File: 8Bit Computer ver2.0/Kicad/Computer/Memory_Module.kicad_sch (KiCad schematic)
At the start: 23 parts, among them IC2 MP2338GTL-Z, J25 M20-8890845, J26 M20-8890845, J27 M20-8890845, J28 M20-8890845, J29 M20-8890845, J30 M20-8890845, J31 M20-8890845

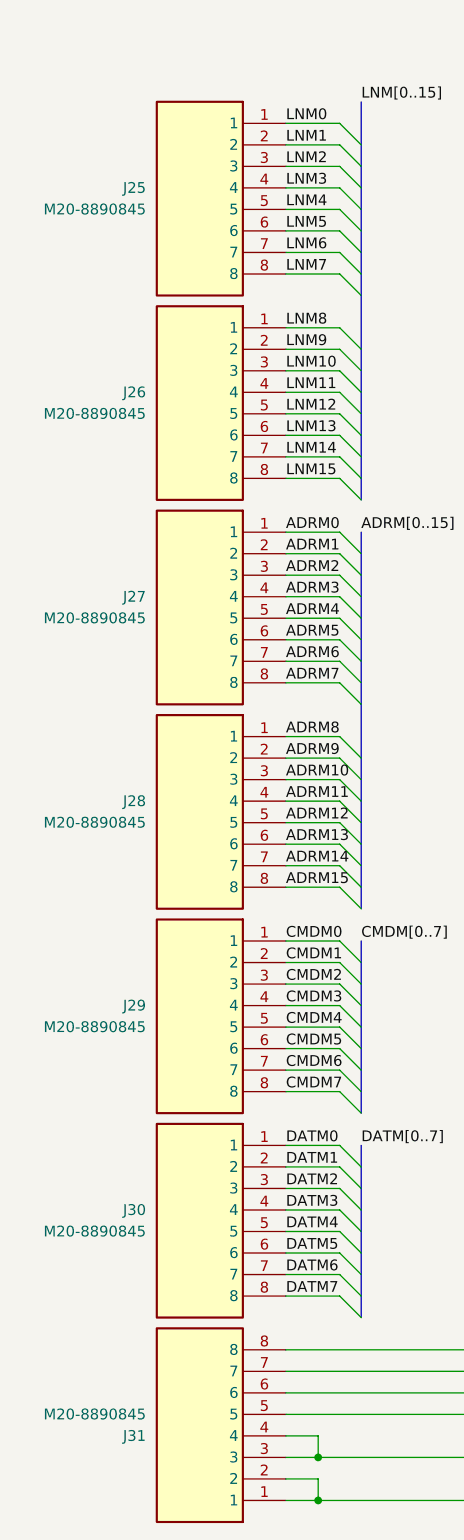
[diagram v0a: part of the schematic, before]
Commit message: changed page numbers, every schematic is now A4
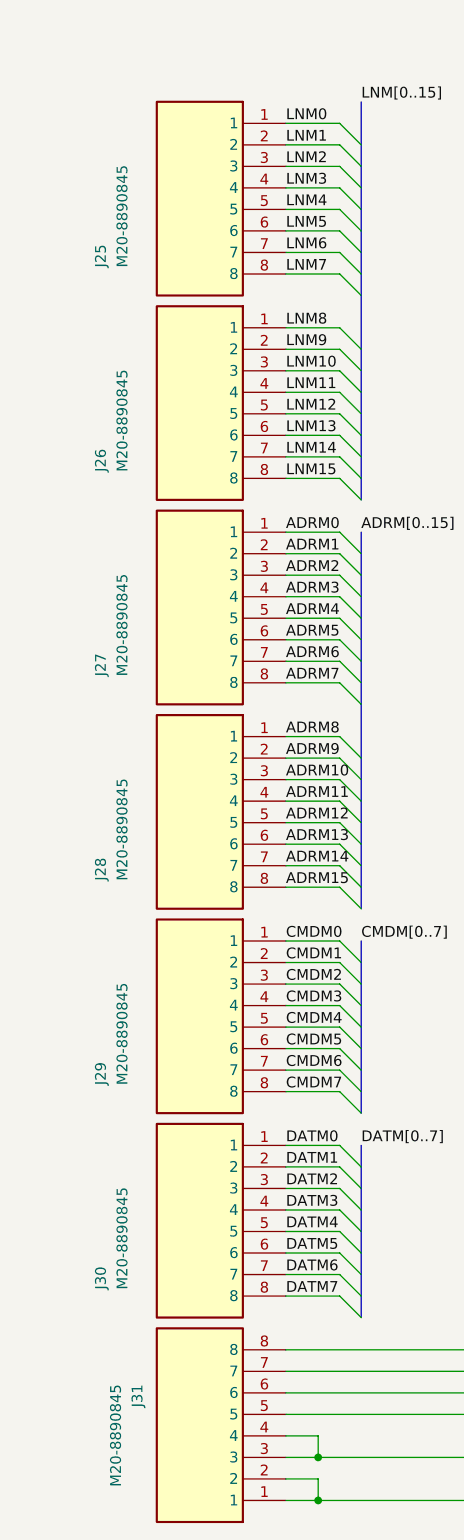
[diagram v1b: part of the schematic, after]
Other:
- title: (none) -> ${SHEETNAME}
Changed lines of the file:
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@@
 	(generator_version "9.0")
 	(paper "A4")
+	(title_block
+		(title "${SHEETNAME}")
+		(date "2026-03-21")
+		(rev "2.7")
+	)
 	(junction
 		(at 275.59 138.43)
@@
 		(dnp no)
 		(property "Reference" "J29"
-			(at 24.13 129.5399 0)
+			(at 18.796 138.938 90)
 			(effects
 				(font
@@
 		)
 		(property "Value" "M20-8890845"
-			(at 24.13 132.0799 0)
+			(at 21.336 138.938 90)
 			(effects
 				(font
@@
 		(dnp no)
 		(property "Reference" "J26"
-			(at 24.13 57.1499 0)
+			(at 18.796 66.548 90)
 			(effects
 				(font
@@
 		)
 		(property "Value" "M20-8890845"
-			(at 24.13 59.6899 0)
+			(at 21.336 66.548 90)
 			(effects
 				(font
@@
 		(dnp no)
 		(property "Reference" "J30"
-			(at 24.13 153.6699 0)
+			(at 18.796 163.068 90)
 			(effects
 				(font
@@
 		)
 		(property "Value" "M20-8890845"
-			(at 24.13 156.2099 0)
+			(at 21.336 163.068 90)
 			(effects
 				(font
@@
 		(dnp no)
 		(property "Reference" "J28"
-			(at 24.13 105.4099 0)
+			(at 18.796 114.808 90)
 			(effects
 				(font
@@
 		)
 		(property "Value" "M20-8890845"
-			(at 24.13 107.9499 0)
+			(at 21.336 114.808 90)
 			(effects
 				(font
@@
 		(dnp no)
 		(property "Reference" "J31"
-			(at 24.13 180.3401 0)
+			(at 23.114 174.244 90)
 			(effects
 				(font
@@
 		)
 		(property "Value" "M20-8890845"
-			(at 24.13 177.8001 0)
+			(at 20.574 174.244 90)
 			(effects
 				(font
@@
 		(dnp no)
 		(property "Reference" "J25"
-			(at 24.13 33.0199 0)
+			(at 18.796 42.418 90)
 			(effects
 				(font
@@
 		)
 		(property "Value" "M20-8890845"
-			(at 24.13 35.5599 0)
+			(at 21.336 42.418 90)
 			(effects
 				(font
@@
 		(dnp no)
 		(property "Reference" "J27"
-			(at 24.13 81.2799 0)
+			(at 18.796 90.678 90)
 			(effects
 				(font
@@
 		)
 		(property "Value" "M20-8890845"
-			(at 24.13 83.8199 0)
+			(at 21.336 90.678 90)
 			(effects
 				(font
@@
 			(project "Computer"
 				(path "/1196a00e-6878-4d6d-82b7-9e052dfe7c14/13a36bad-d32b-469d-8a9a-941e54d6dd87"
-					(page "26")
+					(page "48")
 				)
 			)
@@
 			(project "Computer"
 				(path "/1196a00e-6878-4d6d-82b7-9e052dfe7c14/13a36bad-d32b-469d-8a9a-941e54d6dd87"
-					(page "23")
+					(page "45")
 				)
 			)
